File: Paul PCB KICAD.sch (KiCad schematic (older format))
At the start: 160 parts, among them J1 USB4085-GF-A_REVA, SW1 SW_Push, U1 ATmega32U4-AU, Y1 16MHz

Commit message: Added Near Final Edge Cut and Positioned Switch footprints
Need to add the diodes and caps and some cleanup
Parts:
- removed J1: USB4085-GF-A_REVA, 4085 USB Connector GCT:GCT_USB4085-GF-A_REVA, symbol USB4085-GF-A_REVA:USB4085-GF-A_REVA
- added USB1: HRO-TYPE-C-31-M-12, Type-C:HRO-TYPE-C-31-M-12, symbol Type-C:HRO-TYPE-C-31-M-12
- MX1: renamed from MX6; footprint (none) -> MX_Only:MXOnly-1U-Hotswap
- MX10: renamed from MX49; footprint (none) -> MX_Only:MXOnly-1U-Hotswap
- MX100: renamed from MX2; footprint (none) -> MX_Only:MXOnly-1.5U-Hotswap
- MX101: renamed from MX7; footprint (none) -> MX_Only:MXOnly-1U-Hotswap
- MX102: renamed from MX12; footprint (none) -> MX_Only:MXOnly-1U-Hotswap
- MX103: renamed from MX17; footprint (none) -> MX_Only:MXOnly-1U-Hotswap
- MX104: renamed from MX21; footprint (none) -> MX_Only:MXOnly-1U-Hotswap
- MX105: renamed from MX26; footprint (none) -> MX_Only:MXOnly-1U-Hotswap
- MX106: renamed from MX31; footprint (none) -> MX_Only:MXOnly-1U-Hotswap
- MX107: renamed from MX36; footprint (none) -> MX_Only:MXOnly-1U-Hotswap
- MX108: renamed from MX40; footprint (none) -> MX_Only:MXOnly-1U-Hotswap
- MX109: renamed from MX45; footprint (none) -> MX_Only:MXOnly-1U-Hotswap
- MX11: renamed from MX54; footprint (none) -> MX_Only:MXOnly-1U-Hotswap
- MX110: renamed from MX50; footprint (none) -> MX_Only:MXOnly-1U-Hotswap
- MX111: renamed from MX55; footprint (none) -> MX_Only:MXOnly-1U-Hotswap
- MX112: renamed from MX60; footprint (none) -> MX_Only:MXOnly-1U-Hotswap
- MX113: renamed from MX65; footprint (none) -> MX_Only:MXOnly-1.5U-Hotswap
- MX114: renamed from MX67; footprint (none) -> Rotary_Encoder:RotaryEncoder_Alps_EC11E-Switch_Vertical_H20mm
- MX12: renamed from MX59; footprint (none) -> MX_Only:MXOnly-1U-Hotswap
- MX13: renamed from MX64; footprint (none) -> MX_Only:MXOnly-1U-Hotswap
- MX14: renamed from MX66; footprint (none) -> MX_Only:MXOnly-1U-Hotswap
- MX2: renamed from MX11; footprint (none) -> MX_Only:MXOnly-1U-Hotswap
- MX200: renamed from MX3; footprint (none) -> MX_Only:MXOnly-1.75U-Hotswap
- MX201: renamed from MX8; footprint (none) -> MX_Only:MXOnly-1U-Hotswap
- MX202: renamed from MX13; footprint (none) -> MX_Only:MXOnly-1U-Hotswap
- MX203: renamed from MX18; footprint (none) -> MX_Only:MXOnly-1U-Hotswap
- MX204: renamed from MX22; footprint (none) -> MX_Only:MXOnly-1U-Hotswap
- MX205: renamed from MX27; footprint (none) -> MX_Only:MXOnly-1U-Hotswap
- MX206: renamed from MX32; footprint (none) -> MX_Only:MXOnly-1U-Hotswap
- MX207: renamed from MX37; footprint (none) -> MX_Only:MXOnly-1U-Hotswap
- MX208: renamed from MX41; footprint (none) -> MX_Only:MXOnly-1U-Hotswap
- MX209: renamed from MX46; footprint (none) -> MX_Only:MXOnly-1U-Hotswap
- MX210: renamed from MX51; footprint (none) -> MX_Only:MXOnly-1U-Hotswap
- MX211: renamed from MX56; footprint (none) -> MX_Only:MXOnly-1U-Hotswap
- MX212: renamed from MX61; footprint (none) -> MX_Only:MXOnly-2.25U-Hotswap
- MX214: renamed from MX68; footprint (none) -> MX_Only:MXOnly-1U-Hotswap
- MX3: renamed from MX16; footprint (none) -> MX_Only:MXOnly-1U-Hotswap
- MX300: renamed from MX4; footprint (none) -> MX_Only:MXOnly-2.25U-Hotswap
- MX301: renamed from MX9; footprint (none) -> MX_Only:MXOnly-1U-Hotswap
- MX302: renamed from MX14; footprint (none) -> MX_Only:MXOnly-1U-Hotswap
- MX303: renamed from MX19; footprint (none) -> MX_Only:MXOnly-1U-Hotswap
- MX304: renamed from MX23; footprint (none) -> MX_Only:MXOnly-1U-Hotswap
- MX305: renamed from MX28; footprint (none) -> MX_Only:MXOnly-1U-Hotswap
- MX306: renamed from MX33; footprint (none) -> MX_Only:MXOnly-1U-Hotswap
- MX307: renamed from MX38; footprint (none) -> MX_Only:MXOnly-1U-Hotswap
- MX308: renamed from MX42; footprint (none) -> MX_Only:MXOnly-1U-Hotswap
- MX309: renamed from MX47; footprint (none) -> MX_Only:MXOnly-1U-Hotswap
- MX310: renamed from MX52; footprint (none) -> MX_Only:MXOnly-1U-Hotswap
- MX311: renamed from MX57; footprint (none) -> MX_Only:MXOnly-1U-Hotswap
- MX312: renamed from MX62; footprint (none) -> MX_Only:MXOnly-1U-Hotswap
- MX314: renamed from MX69; footprint (none) -> MX_Only:MXOnly-1U-Hotswap
- MX4: renamed from MX20; footprint (none) -> MX_Only:MXOnly-1U-Hotswap
- MX400: renamed from MX5; footprint (none) -> MX_Only:MXOnly-1.25U-Hotswap
- MX401: renamed from MX10; footprint (none) -> MX_Only:MXOnly-1.25U-Hotswap
- MX402: renamed from MX15; footprint (none) -> MX_Only:MXOnly-1.25U-Hotswap
- MX404: renamed from MX24; footprint (none) -> MX_Only:MXOnly-2.75U-Hotswap-ReversedStabilizers
- MX405: renamed from MX29; footprint (none) -> MX_Only:MXOnly-1U-Hotswap
- MX406: renamed from MX34; footprint (none) -> MX_Only:MXOnly-2.25U-Hotswap-ReversedStabilizers
- MX408: renamed from MX43; footprint (none) -> MX_Only:MXOnly-1U-Hotswap
- MX409: renamed from MX48; footprint (none) -> MX_Only:MXOnly-1U-Hotswap
- MX410: renamed from MX53; footprint (none) -> MX_Only:MXOnly-1U-Hotswap
- MX411: renamed from MX58; footprint (none) -> MX_Only:MXOnly-1U-Hotswap
- MX412: renamed from MX63; footprint (none) -> MX_Only:MXOnly-1U-Hotswap
- MX414: renamed from MX70; footprint (none) -> MX_Only:MXOnly-1U-Hotswap
- MX5: renamed from MX25; footprint (none) -> MX_Only:MXOnly-1U-Hotswap
- MX6: renamed from MX30; footprint (none) -> MX_Only:MXOnly-1U-Hotswap
- MX7: renamed from MX35; footprint (none) -> MX_Only:MXOnly-1U-Hotswap
- MX8: renamed from MX39; footprint (none) -> MX_Only:MXOnly-1U-Hotswap
- MX9: renamed from MX44; footprint (none) -> MX_Only:MXOnly-1U-Hotswap
- renumbered D1 to D0, D6 to D1, D49 to D10, D2 to D100, D7 to D101, D12 to D102, D17 to D103, D21 to D104, D26 to D105, D31 to D106, D36 to D107, D40 to D108, D45 to D109, D54 to D11, D50 to D110, D55 to D111, D60 to D112, D65 to D113, D67 to D114, D59 to D12, D64 to D13, D66 to D14, D11 to D2, D3 to D200, D8 to D201, D13 to D202, D18 to D203, D22 to D204, D27 to D205, D32 to D206, D37 to D207, D41 to D208, D46 to D209, D51 to D210, D56 to D211, D61 to D212, D68 to D214, D16 to D3, D4 to D300, D9 to D301, D14 to D302, D19 to D303, D23 to D304, D28 to D305, D33 to D306, D38 to D307, D42 to D308, D47 to D309, D52 to D310, D57 to D311, D62 to D312, D69 to D314, D20 to D4, D5 to D400, D10 to D401, D15 to D402, D24 to D404, D29 to D405, D34 to D406, D43 to D408, D48 to D409, D53 to D410, D58 to D411, D63 to D412, D70 to D414, D25 to D5, D30 to D6, D35 to D7, D39 to D8, D44 to D9, MX1 to MX0
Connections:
- net D+: now also USB1.6 (DP1), USB1.8 (DP2)
- net D-: now also USB1.5 (DN2), USB1.7 (DN1)
- net GND: now also USB1.1 (GND), USB1.12 (GND); no longer U1.15 (GND), U1.23 (GND), U1.35 (GND), U1.43 (GND)
- net VCC: now also USB1.11 (VBUS), USB1.2 (VBUS)
- net at R3.2: now also USB1.10 (CC2)
- net at R2.2: now also USB1.4 (CC1)
- net at C1.2, R1.2: now also USB1.13 (SHIELD)
- new net: U1.15 (GND), U1.23 (GND), U1.35 (GND), U1.43 (GND)
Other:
- moved on the sheet: C2, C5, C6, C8, D0, D1, D10, D100, D101, D102, D103, D104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

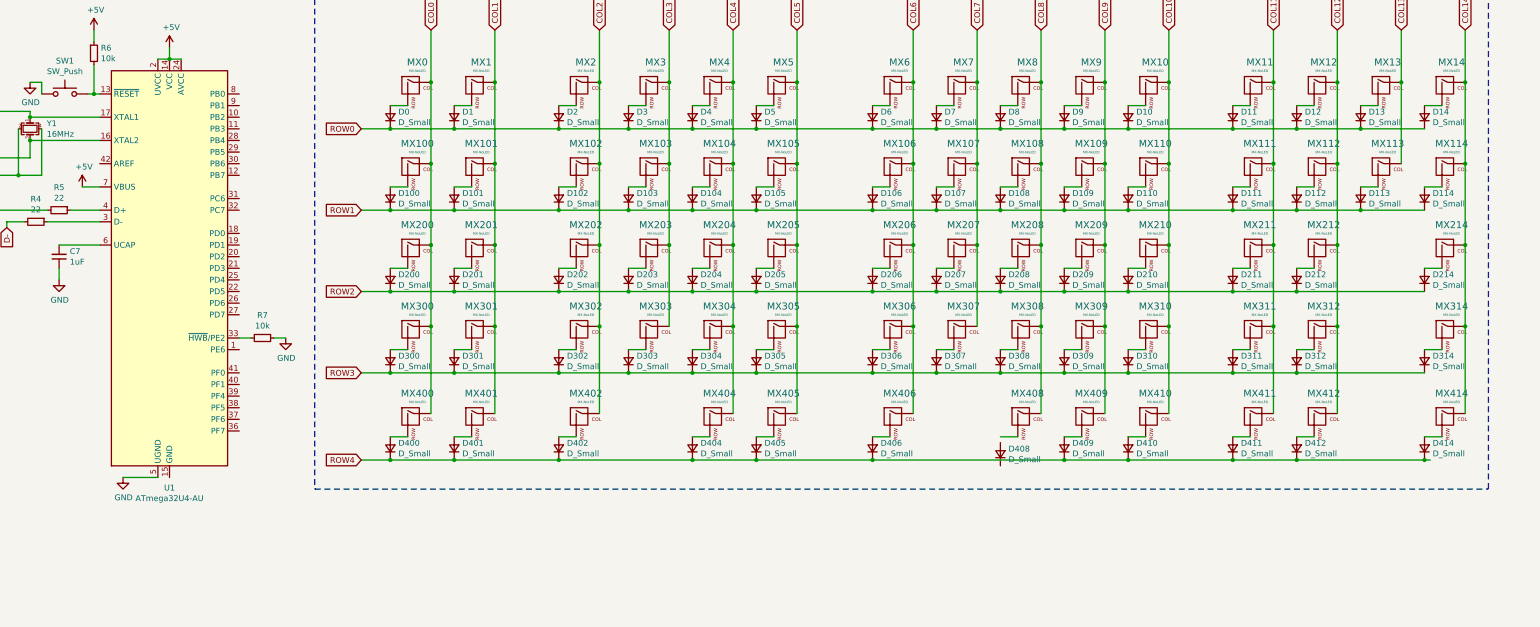
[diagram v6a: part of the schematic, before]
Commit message: More PCB Completed
Added Mounting Holes as pads
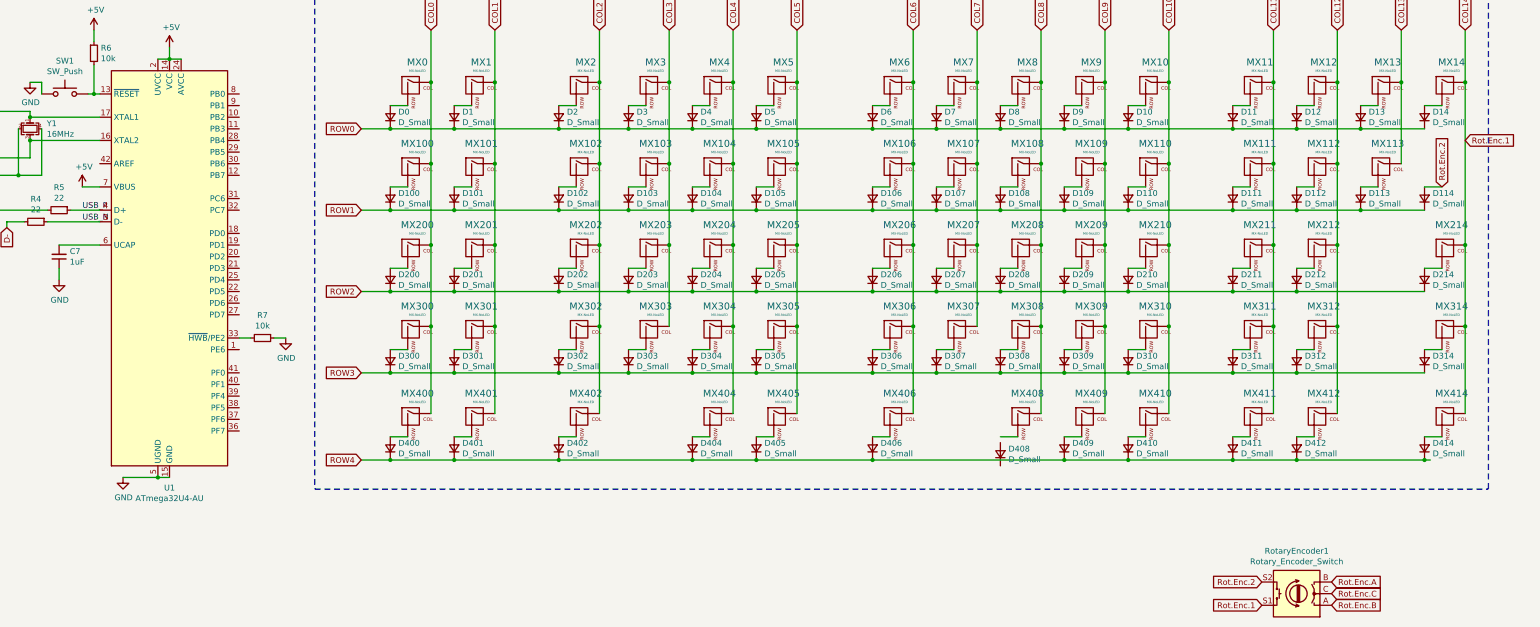
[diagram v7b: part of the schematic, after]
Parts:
- removed MX114: MX-NoLED, Rotary_Encoder:RotaryEncoder_Alps_EC11E-Switch_Vertical_H20mm, symbol MX_Alps_Hybrid:MX-NoLED
- added RotaryEncoder1: Rotary_Encoder_Switch, Rotary_Encoder:RotaryEncoder_Alps_EC11E-Switch_Vertical_H20mm, symbol Device:Rotary_Encoder_Switch
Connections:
- net COL14: now also RotaryEncoder1.S1
- net GND: now also U1.15 (GND), U1.23 (GND), U1.35 (GND), U1.43 (GND)
- net USB_N: now reaches R4.1, U1.3 (D-)
- net USB_P: now reaches R5.1, U1.4 (D+)
- net Rot.Enc.2: now reaches D114.2 (A)
- net Rot.Enc.2: now also RotaryEncoder1.S2
- new net Rot.Enc.A: RotaryEncoder1.B
- new net Rot.Enc.B: RotaryEncoder1.A
- new net Rot.Enc.C: RotaryEncoder1.C
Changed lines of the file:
@@
 	1850 2200 1900 2200
-$Comp
-L MX_Alps_Hybrid:MX-NoLED MX0
-U 1 1 607E1287
-P 6550 2000
-F 0 "MX0" H 6583 2223 60  0000 C CNN
-F 1 "MX-NoLED" H 6583 2149 20  0000 C CNN
-F 2 "MX_Only:MXOnly-1U-Hotswap" H 5925 1975 60  0001 C CNN
-F 3 "" H 5925 1975 60  0001 C CNN
-	1    6550 2000
-	1    0    0    -1
-$EndComp
 $Comp
 L Device:D_Small D0
@@
 	6500 2150 6350 2150
 $Comp
-L MX_Alps_Hybrid:MX-NoLED MX1
-U 1 1 607F33E0
-P 7100 2000
-F 0 "MX1" H 7133 2223 60  0000 C CNN
-F 1 "MX-NoLED" H 7133 2149 20  0000 C CNN
-F 2 "MX_Only:MXOnly-1U-Hotswap" H 6475 1975 60  0001 C CNN
-F 3 "" H 6475 1975 60  0001 C CNN
-	1    7100 2000
-	1    0    0    -1
-$EndComp
-$Comp
 L Device:D_Small D1
 U 1 1 607F33E6
@@
 Wire Wire Line
 	7050 5000 6900 5000
-$Comp
-L MX_Alps_Hybrid:MX-NoLED MX2
-U 1 1 60815E60
-P 8000 2000
-F 0 "MX2" H 8033 2223 60  0000 C CNN
-F 1 "MX-NoLED" H 8033 2149 20  0000 C CNN
-F 2 "MX_Only:MXOnly-1U-Hotswap" H 7375 1975 60  0001 C CNN
-F 3 "" H 7375 1975 60  0001 C CNN
-	1    8000 2000
-	1    0    0    -1
-$EndComp
 $Comp
 L Device:D_Small D2
@@
 	15400 2150 15250 2150
 $Comp
-L MX_Alps_Hybrid:MX-NoLED MX114
-U 1 1 608C27ED
-P 15450 2700
-F 0 "MX114" H 15483 2923 60  0000 C CNN
-F 1 "MX-NoLED" H 15483 2849 20  0000 C CNN
-F 2 "Rotary_Encoder:RotaryEncoder_Alps_EC11E-Switch_Vertical_H20mm" H 14825 2675 60  0001 C CNN
-F 3 "" H 14825 2675 60  0001 C CNN
-	1    15450 2700
-	1    0    0    -1
-$EndComp
-$Comp
 L Device:D_Small D114
 U 1 1 608C27F3
@@
 	15600 1500 15600 1950
 Connection ~ 15600 1950
-Wire Wire Line
-	15600 1950 15600 2650
-Connection ~ 15600 2650
-Wire Wire Line
-	15600 2650 15600 3350
 Connection ~ 15600 3350
 Wire Wire Line
@@
 Wire Wire Line
 	4050 5350 4350 5350
+$Comp
+L MX_Alps_Hybrid:MX-NoLED MX2
+U 1 1 60815E60
+P 8000 2000
+F 0 "MX2" H 8033 2223 60  0000 C CNN
+F 1 "MX-NoLED" H 8033 2149 20  0000 C CNN
+F 2 "MX_Only:MXOnly-1U-Hotswap" H 7375 1975 60  0001 C CNN
+F 3 "" H 7375 1975 60  0001 C CNN
+	1    8000 2000
+	1    0    0    -1
+$EndComp
+$Comp
+L MX_Alps_Hybrid:MX-NoLED MX1
+U 1 1 607F33E0
+P 7100 2000
+F 0 "MX1" H 7133 2223 60  0000 C CNN
+F 1 "MX-NoLED" H 7133 2149 20  0000 C CNN
+F 2 "MX_Only:MXOnly-1U-Hotswap" H 6475 1975 60  0001 C CNN
+F 3 "" H 6475 1975 60  0001 C CNN
+	1    7100 2000
+	1    0    0    -1
+$EndComp
+$Comp
+L MX_Alps_Hybrid:MX-NoLED MX0
+U 1 1 607E1287
+P 6550 2000
+F 0 "MX0" H 6583 2223 60  0000 C CNN
+F 1 "MX-NoLED" H 6583 2149 20  0000 C CNN
+F 2 "MX_Only:MXOnly-1U-Hotswap" H 5925 1975 60  0001 C CNN
+F 3 "" H 5925 1975 60  0001 C CNN
+	1    6550 2000
+	1    0    0    -1
+$EndComp
+$Comp
+L Device:Rotary_Encoder_Switch RotaryEncoder1
+U 1 1 60CFC5D9
+P 14150 6350
+F 0 "RotaryEncoder1" H 14150 5983 50  0000 C CNN
+F 1 "Rotary_Encoder_Switch" H 14150 6074 50  0000 C CNN
+F 2 "Rotary_Encoder:RotaryEncoder_Alps_EC11E-Switch_Vertical_H20mm" H 14000 6510 50  0001 C CNN
+F 3 "~" H 14150 6610 50  0001 C CNN
+	1    14150 6350
+	-1   0    0    1
+$EndComp
+Wire Wire Line
+	15600 1950 15600 3350
+Text GLabel 15600 2450 2    50   Input ~ 0
+Rot.Enc.1
+Text GLabel 15400 2850 1    50   Input ~ 0
+Rot.Enc.2
+Text GLabel 13850 6450 0    50   Input ~ 0
+Rot.Enc.1
+Text GLabel 13850 6250 0    50   Input ~ 0
+Rot.Enc.2
+Text GLabel 14450 6250 2    50   Input ~ 0
+Rot.Enc.A
+Text GLabel 14450 6350 2    50   Input ~ 0
+Rot.Enc.C
+Text GLabel 14450 6450 2    50   Input ~ 0
+Rot.Enc.B
+Wire Wire Line
+	4450 5350 4350 5350
+Connection ~ 4350 5350
+Text Label 3700 3050 0    50   ~ 0
+USB_P
+Text Label 3700 3150 0    50   ~ 0
+USB_N
 $EndSCHEMATC

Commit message: Further Completion
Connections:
- net Reset: now reaches R6.2, SW1.2, U1.13 (~RESET)
- net USB_N renamed Data_N
- net USB_P renamed Data_P
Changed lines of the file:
@@
 Connection ~ 4350 5350
 Text Label 3700 3050 0    50   ~ 0
+Data_P
+Text Label 3700 3150 0    50   ~ 0
+Data_N
+Text Label 3800 2050 0    50   ~ 0
+Reset
+Text Label 2950 3050 0    50   ~ 0
 USB_P
-Text Label 3700 3150 0    50   ~ 0
+Text Label 3050 3150 0    50   ~ 0
 USB_N
 $EndSCHEMATC
